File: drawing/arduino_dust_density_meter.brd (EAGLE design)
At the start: 147.3 x 86 mm, 7 parts

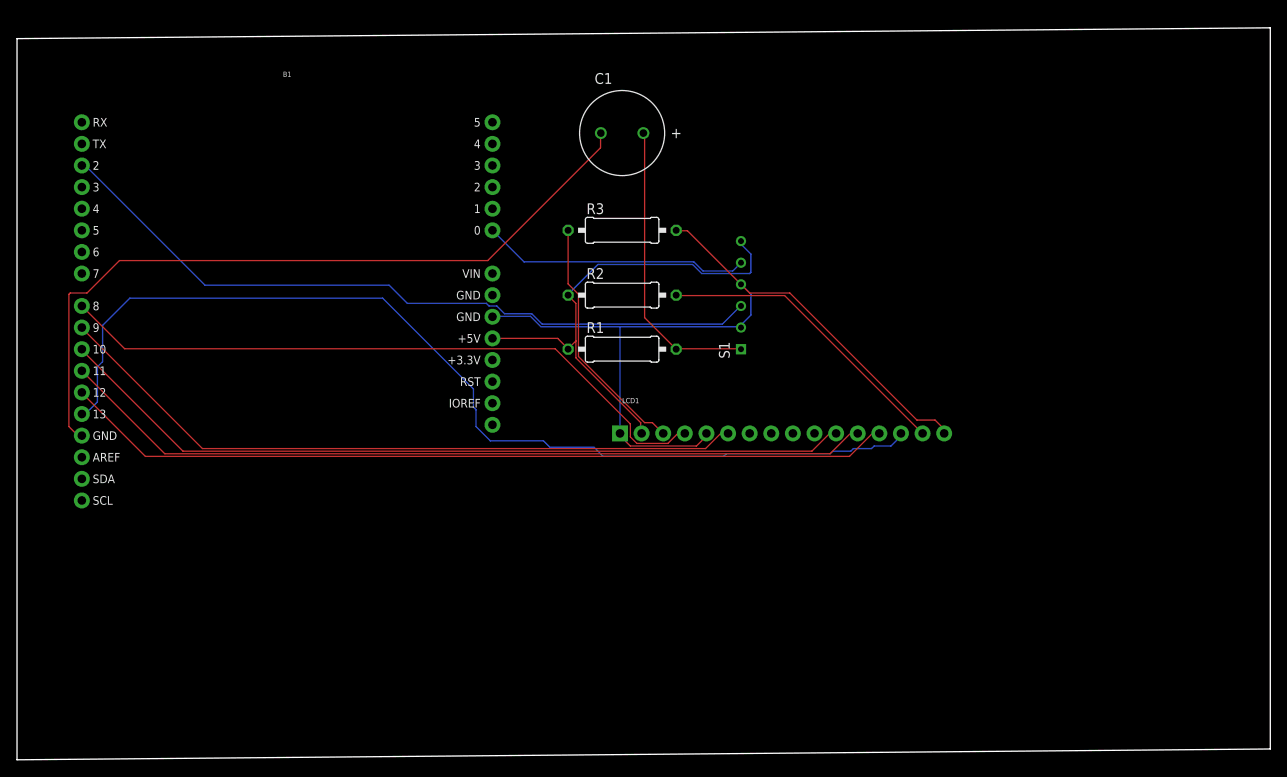
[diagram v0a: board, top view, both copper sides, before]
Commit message: [REFACTOR] Change sensor library
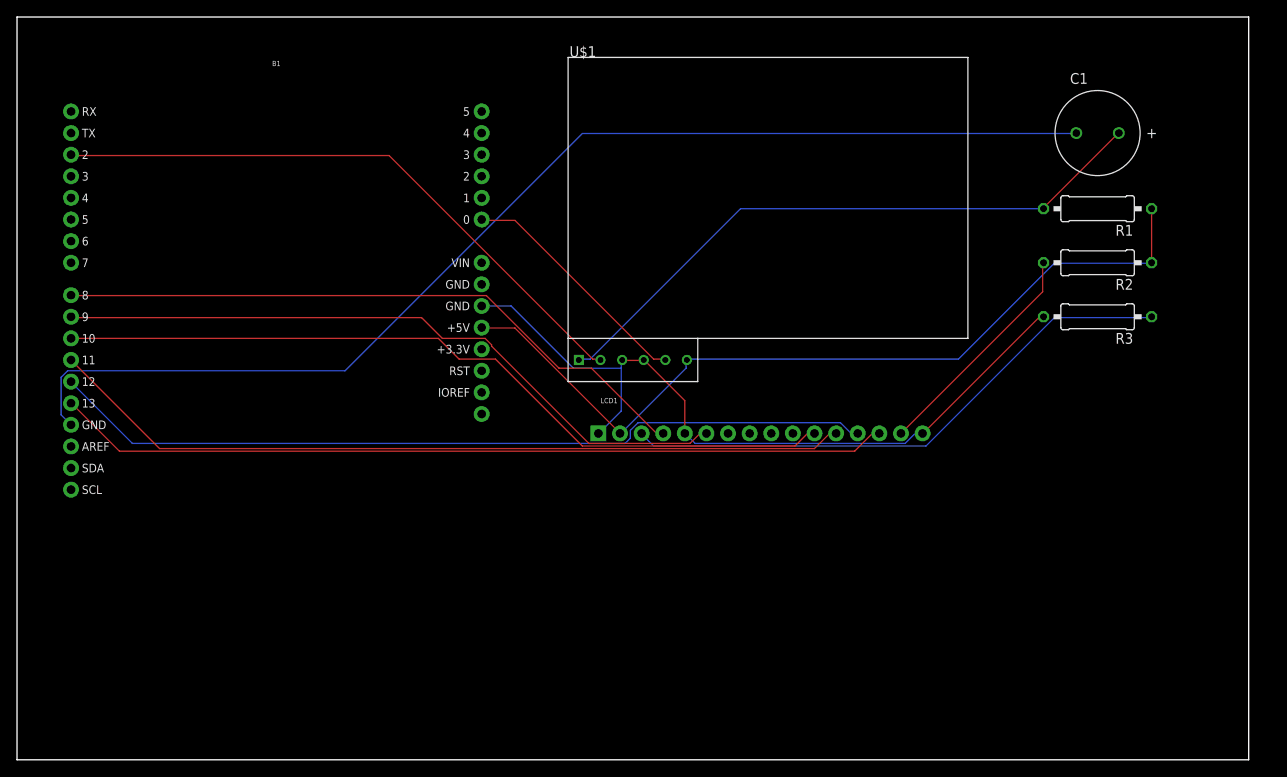
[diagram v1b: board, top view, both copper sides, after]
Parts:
- removed S1: GP2Y1014AU0F, sharp-dust-sensor:GP2Y1014AU0F
- added U$1: GP2Y1014AU0F, sharp-dust-sensor:GP2Y1014AU0F
- moved R1 58.3 mm to (127.0, 64.8), turned to 180 degrees
- moved R3 56.8 mm to (127.0, 52.1), turned to 180 degrees
- moved R2 56.0 mm to (127.0, 58.4), turned to 180 degrees
- moved C1 55.9 mm to (127.0, 73.7)
- moved LCD1 2.54 mm to (100.3, 22.9)
- moved B1 1.80 mm to (30.5, 50.8)
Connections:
- net N$1: now also U$1.V-LED1; no longer S1.V-LED
- net N$2: now also U$1.VCC1; no longer S1.VCC
- net N$4: now also U$1.LED1, U$1.S-GND1; no longer S1.LED-GND, S1.S-GND
- net N$5: now also U$1.LED-GND1; no longer S1.LED
- net N$6: now also U$1.VO1; no longer S1.VO
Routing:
- net N$3: track 88.9 -> 137.3 mm
- net N$2: track 58.3 -> 99.1 mm
- net N$1: track 34.7 -> 74.7 mm
- net N$14: track 29.0 -> 66.9 mm
- net N$7: track 118.3 -> 98.3 mm
- net N$5: track 86.1 -> 72.3 mm
- net N$4: track 101.8 -> 91.3 mm
- net N$13: track 35.7 -> 27.0 mm
- net N$6: track 31.6 -> 28.5 mm
- net N$12: track 79.0 -> 76.3 mm
- net N$9: track 96.2 -> 95.0 mm
- net N$10: track 94.5 -> 93.3 mm
- net N$11: track 82.6 -> 81.4 mm
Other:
- board size 147.3 x 86 mm -> 144.8 x 87.3 mm
